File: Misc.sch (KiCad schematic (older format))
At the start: 25 parts, among them U3 PCF8523TK, U4 TLV70218DBV, U5 CDCE913PW, U7 LM75BDP, U8 LM75BDP, X1 32768, X2 20MHz

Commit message: Squiggles! Silk!
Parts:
- renumbered BT1 to BT701, C83 to C701, C84 to C702, C85 to C703, C88 to C704, C86 to C705, C144 to C706, C87 to C707, C123 to C708, C124 to C709, C89 to C710, C142 to C711, C143 to C712, R85 to R701, R88 to R702, R89 to R703, R90 to R704, R91 to R705, U4 to U701, U3 to U702, U7 to U703, U8 to U704, U5 to U705, X2 to X701, X1 to X702

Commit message: Final BOM
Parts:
- added C713, C714: 10p, IPC7351-Nominal:CAPC1005X55, symbol C-0402
- added R706: 1k, IPC7351-Nominal:RESC1005X40, symbol R-0402
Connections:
- net GND: now also C713.2, C714.2
- net at C707.1, U702.3 (VBAT): now also R706.1; no longer BT701.1 (+)
- net at U705.1 (Xin/CLK), X701.1: now also C714.1
- net at U705.14 (Xout), X701.2: now also C713.1
- new net: BT701.1 (+), R706.2
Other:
- moved on the sheet: BT701
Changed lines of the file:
@@
 $EndComp
 $Comp
-L GND #PWR722
+L GND #PWR723
 U 1 1 57983039
 P 6850 1700
-F 0 "#PWR722" H 6850 1700 30  0001 C CNN
+F 0 "#PWR723" H 6850 1700 30  0001 C CNN
 F 1 "GND" H 6850 1630 30  0001 C CNN
 F 2 "" H 6850 1700 60  0000 C CNN
@@
 L BATTERY-SHORT BT701
 U 1 1 579852CE
-P 3800 1800
-F 0 "BT701" H 3940 1821 50  0000 L CNN
-F 1 "3V" H 3940 1730 50  0000 L CNN
-F 2 "manuf:MPD-BU2032SM-HD-G" H 3800 1700 60  0001 C CNN
-F 3 "" H 3800 1700 60  0000 C CNN
-F 4 "DIST DIGIKEY BU2032SM-HD-GCT-ND" H 3800 1800 60  0001 C CNN "BOM"
-	1    3800 1800
+P 3550 1800
+F 0 "BT701" H 3690 1821 50  0000 L CNN
+F 1 "3V" H 3690 1730 50  0000 L CNN
+F 2 "manuf:MPD-BU2032SM-HD-G" H 3550 1700 60  0001 C CNN
+F 3 "" H 3550 1700 60  0000 C CNN
+F 4 "DIST DIGIKEY BU2032SM-HD-GCT-ND" H 3550 1800 60  0001 C CNN "BOM"
+	1    3550 1800
 	1    0    0    -1
 $EndComp
@@
 L GND #PWR708
 U 1 1 5798538F
-P 3800 2000
-F 0 "#PWR708" H 3800 2000 30  0001 C CNN
-F 1 "GND" H 3800 1930 30  0001 C CNN
-F 2 "" H 3800 2000 60  0000 C CNN
-F 3 "" H 3800 2000 60  0000 C CNN
-	1    3800 2000
+P 3550 2000
+F 0 "#PWR708" H 3550 2000 30  0001 C CNN
+F 1 "GND" H 3550 1930 30  0001 C CNN
+F 2 "" H 3550 2000 60  0000 C CNN
+F 3 "" H 3550 2000 60  0000 C CNN
+	1    3550 2000
 	1    0    0    -1
 $EndComp
@@
 CLK_CPU
 $Comp
-L GND #PWR723
+L GND #PWR724
 U 1 1 5798C21D
 P 7900 4100
-F 0 "#PWR723" H 7900 4100 30  0001 C CNN
+F 0 "#PWR724" H 7900 4100 30  0001 C CNN
 F 1 "GND" H 7900 4030 30  0001 C CNN
 F 2 "" H 7900 4100 60  0000 C CNN
@@
 $EndComp
 $Comp
-L GND #PWR724
+L GND #PWR725
 U 1 1 57A157A8
 P 8600 3600
-F 0 "#PWR724" H 8600 3600 30  0001 C CNN
+F 0 "#PWR725" H 8600 3600 30  0001 C CNN
 F 1 "GND" H 8600 3530 30  0001 C CNN
 F 2 "" H 8600 3600 60  0000 C CNN
@@
 $EndComp
 $Comp
-L GND #PWR725
+L GND #PWR726
 U 1 1 57A158A4
 P 8900 3600
-F 0 "#PWR725" H 8900 3600 30  0001 C CNN
+F 0 "#PWR726" H 8900 3600 30  0001 C CNN
 F 1 "GND" H 8900 3530 30  0001 C CNN
 F 2 "" H 8900 3600 60  0000 C CNN
@@
 $EndComp
 $Comp
-L GND #PWR721
+L GND #PWR722
 U 1 1 57A177C2
 P 6350 3250
-F 0 "#PWR721" H 6350 3250 30  0001 C CNN
+F 0 "#PWR722" H 6350 3250 30  0001 C CNN
 F 1 "GND" H 6350 3180 30  0001 C CNN
 F 2 "" H 6350 3250 60  0000 C CNN
@@
 $EndComp
 $Comp
-L GND #PWR719
+L GND #PWR720
 U 1 1 57B04C9B
 P 5800 4200
-F 0 "#PWR719" H 5800 4200 30  0001 C CNN
+F 0 "#PWR720" H 5800 4200 30  0001 C CNN
 F 1 "GND" H 5800 4130 30  0001 C CNN
 F 2 "" H 5800 4200 60  0000 C CNN
@@
 $EndComp
 $Comp
-L GND #PWR720
+L GND #PWR721
 U 1 1 57B04D81
 P 6200 4200
-F 0 "#PWR720" H 6200 4200 30  0001 C CNN
+F 0 "#PWR721" H 6200 4200 30  0001 C CNN
 F 1 "GND" H 6200 4130 30  0001 C CNN
 F 2 "" H 6200 4200 60  0000 C CNN
@@
 L PWR #PWR711
 U 1 1 57B027DE
-P 4600 1650
-F 0 "#PWR711" H 4600 1650 50  0001 C CNN
-F 1 "PWR" H 4600 1650 50  0001 C CNN
-F 2 "" H 4600 1650 60  0000 C CNN
-F 3 "" H 4600 1650 60  0000 C CNN
-	1    4600 1650
+P 4700 1650
+F 0 "#PWR711" H 4700 1650 50  0001 C CNN
+F 1 "PWR" H 4700 1650 50  0001 C CNN
+F 2 "" H 4700 1650 60  0000 C CNN
+F 3 "" H 4700 1650 60  0000 C CNN
+	1    4700 1650
 	-1   0    0    1
 $EndComp
@@
 	4800 1900 4800 2300
 Wire Wire Line
-	3800 1600 5000 1600
-Wire Wire Line
-	3800 1600 3800 1700
-Wire Wire Line
-	3800 2000 3800 1950
+	4150 1600 5000 1600
+Wire Wire Line
+	3550 1600 3550 1700
+Wire Wire Line
+	3550 2000 3550 1950
 Wire Wire Line
 	4300 1700 4300 1600
@@
 	8900 3600 8900 3500
 Wire Wire Line
-	6250 3100 6200 3100
+	6050 3100 6250 3100
 Wire Wire Line
 	6450 3100 6800 3100
@@
 Connection ~ 2200 1500
 Wire Wire Line
-	4600 1650 4600 1600
-Connection ~ 4600 1600
+	4700 1650 4700 1600
+Connection ~ 4700 1600
+$Comp
+L C-0402 C?
+U 1 1 57B0B7B1
+P 5950 2700
+AR Path="/57B0B7B1" Ref="C?"  Part="1"
+AR Path="/5765C2BD/57B0B7B1" Ref="C?"  Part="1"
+AR Path="/57981212/57B0B7B1" Ref="C713"  Part="1"
+F 0 "C713" V 5700 2700 50  0000 C CNN
+F 1 "10p" V 5791 2700 50  0000 C CNN
+F 2 "IPC7351-Nominal:CAPC1005X55" H 5950 2700 50  0001 C CNN
+F 3 "" H 5940 2675 60  0000 C CNN
+F 4 "CAP MLCC 10p C0G [0402]" H 6750 3250 60  0001 C CNN "BOM"
+	1    5950 2700
+	0    1    1    0
+$EndComp
+$Comp
+L C-0402 C?
+U 1 1 57B0B99F
+P 5950 3100
+AR Path="/57B0B99F" Ref="C?"  Part="1"
+AR Path="/5765C2BD/57B0B99F" Ref="C?"  Part="1"
+AR Path="/57981212/57B0B99F" Ref="C714"  Part="1"
+F 0 "C714" V 5700 3100 50  0000 C CNN
+F 1 "10p" V 5791 3100 50  0000 C CNN
+F 2 "IPC7351-Nominal:CAPC1005X55" H 5950 3100 50  0001 C CNN
+F 3 "" H 5940 3075 60  0000 C CNN
+F 4 "CAP MLCC 10p C0G [0402]" H 6750 3650 60  0001 C CNN "BOM"
+	1    5950 3100
+	0    1    1    0
+$EndComp
+Connection ~ 6200 3100
+Wire Wire Line
+	6050 2700 6550 2700
+Wire Wire Line
+	6550 2700 6550 3100
+Connection ~ 6550 3100
+Wire Wire Line
+	5850 2700 5750 2700
+Wire Wire Line
+	5750 2700 5750 3100
+Wire Wire Line
+	5750 3100 5850 3100
+$Comp
+L GND #PWR719
+U 1 1 57B0BDB7
+P 5650 2900
+F 0 "#PWR719" H 5650 2900 30  0001 C CNN
+F 1 "GND" H 5650 2830 30  0001 C CNN
+F 2 "" H 5650 2900 60  0000 C CNN
+F 3 "" H 5650 2900 60  0000 C CNN
+	1    5650 2900
+	0    1    1    0
+$EndComp
+Wire Wire Line
+	5650 2900 5750 2900
+Connection ~ 5750 2900
+$Comp
+L R-0402 R706
+U 1 1 57B0F234
+P 4050 1600
+F 0 "R706" V 4158 1600 50  0000 C CNN
+F 1 "1k" V 4249 1600 50  0000 C CNN
+F 2 "IPC7351-Nominal:RESC1005X40" H 4050 1600 50  0001 C CNN
+F 3 "" H 4050 1650 60  0000 C CNN
+F 4 "RES SMD 1k 1% [0402]" H 4800 2150 60  0001 C CNN "BOM"
+	1    4050 1600
+	0    1    1    0
+$EndComp
+Wire Wire Line
+	3950 1600 3550 1600
 $EndSCHEMATC

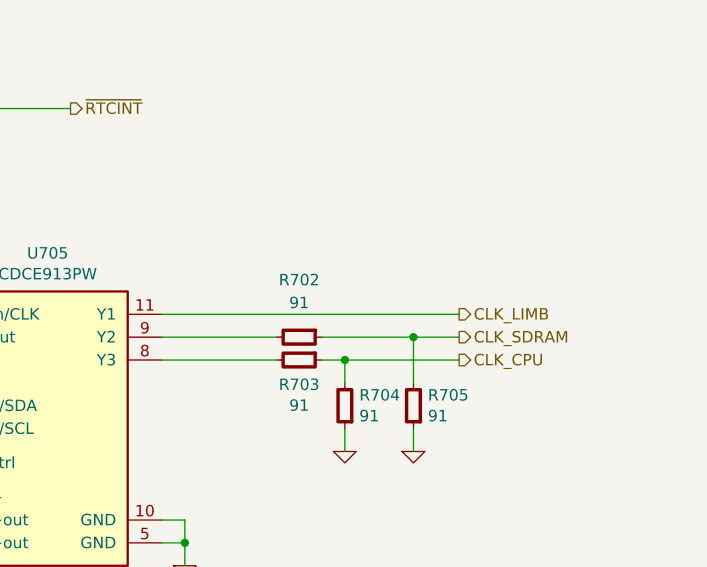
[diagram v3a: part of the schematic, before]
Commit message: Add some test points
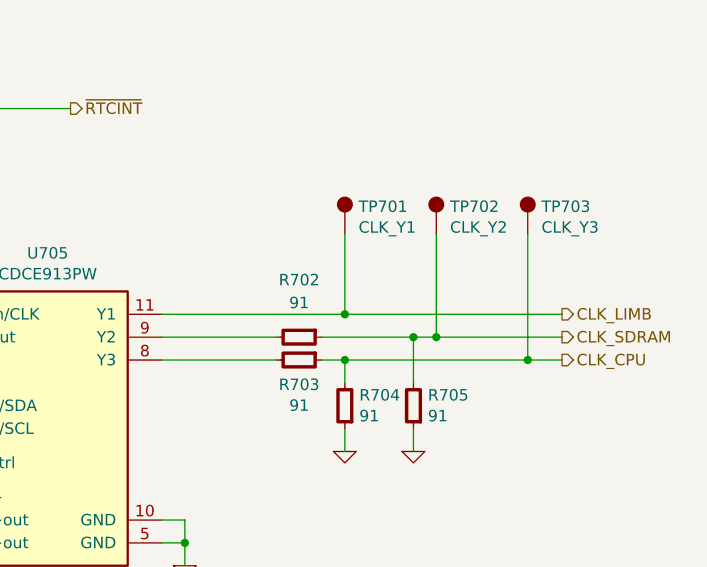
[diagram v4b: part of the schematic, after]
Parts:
- added TP701: CLK_Y1, conn-test:TEST-SMD-SMALL, symbol TESTPOINT
- added TP702: CLK_Y2, conn-test:TEST-SMD-SMALL, symbol TESTPOINT
- added TP703: CLK_Y3, conn-test:TEST-SMD-SMALL, symbol TESTPOINT
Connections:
- net CLK_CPU: now also TP703.1
- net CLK_LIMB: now also TP701.1
- net CLK_SDRAM: now also TP702.1
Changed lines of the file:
@@
 	1    0    0    -1
 $EndComp
-Text HLabel 9100 3000 2    50   Output ~ 0
+Text HLabel 9550 3000 2    50   Output ~ 0
 CLK_LIMB
-Text HLabel 9100 3100 2    50   Output ~ 0
+Text HLabel 9550 3100 2    50   Output ~ 0
 CLK_SDRAM
-Text HLabel 9100 3200 2    50   Output ~ 0
+Text HLabel 9550 3200 2    50   Output ~ 0
 CLK_CPU
 $Comp
@@
 	4800 6700 4800 6600
 Wire Wire Line
-	7800 3000 9100 3000
+	7800 3000 9550 3000
 Wire Wire Line
 	8300 3100 7800 3100
 Wire Wire Line
-	8500 3100 9100 3100
-Wire Wire Line
-	8500 3200 9100 3200
+	8500 3100 9550 3100
+Wire Wire Line
+	8500 3200 9550 3200
 Wire Wire Line
 	8300 3200 7800 3200
@@
 Wire Wire Line
 	3950 1600 3550 1600
+$Comp
+L TESTPOINT TP701
+U 1 1 57C83404
+P 8600 2650
+F 0 "TP701" H 8660 2771 50  0000 L CNN
+F 1 "CLK_Y1" H 8660 2680 50  0000 L CNN
+F 2 "conn-test:TEST-SMD-SMALL" H 8600 2650 50  0001 C CNN
+F 3 "" H 8600 2650 50  0000 C CNN
+	1    8600 2650
+	1    0    0    -1
+$EndComp
+Wire Wire Line
+	8600 2650 8600 3000
+Connection ~ 8600 3000
+$Comp
+L TESTPOINT TP702
+U 1 1 57C83706
+P 9000 2650
+F 0 "TP702" H 9060 2771 50  0000 L CNN
+F 1 "CLK_Y2" H 9060 2680 50  0000 L CNN
+F 2 "conn-test:TEST-SMD-SMALL" H 9000 2650 50  0001 C CNN
+F 3 "" H 9000 2650 50  0000 C CNN
+	1    9000 2650
+	1    0    0    -1
+$EndComp
+$Comp
+L TESTPOINT TP703
+U 1 1 57C8377C
+P 9400 2650
+F 0 "TP703" H 9460 2771 50  0000 L CNN
+F 1 "CLK_Y3" H 9460 2680 50  0000 L CNN
+F 2 "conn-test:TEST-SMD-SMALL" H 9400 2650 50  0001 C CNN
+F 3 "" H 9400 2650 50  0000 C CNN
+	1    9400 2650
+	1    0    0    -1
+$EndComp
+Wire Wire Line
+	9000 2650 9000 3100
+Connection ~ 9000 3100
+Wire Wire Line
+	9400 2650 9400 3200
+Connection ~ 9400 3200
 $EndSCHEMATC

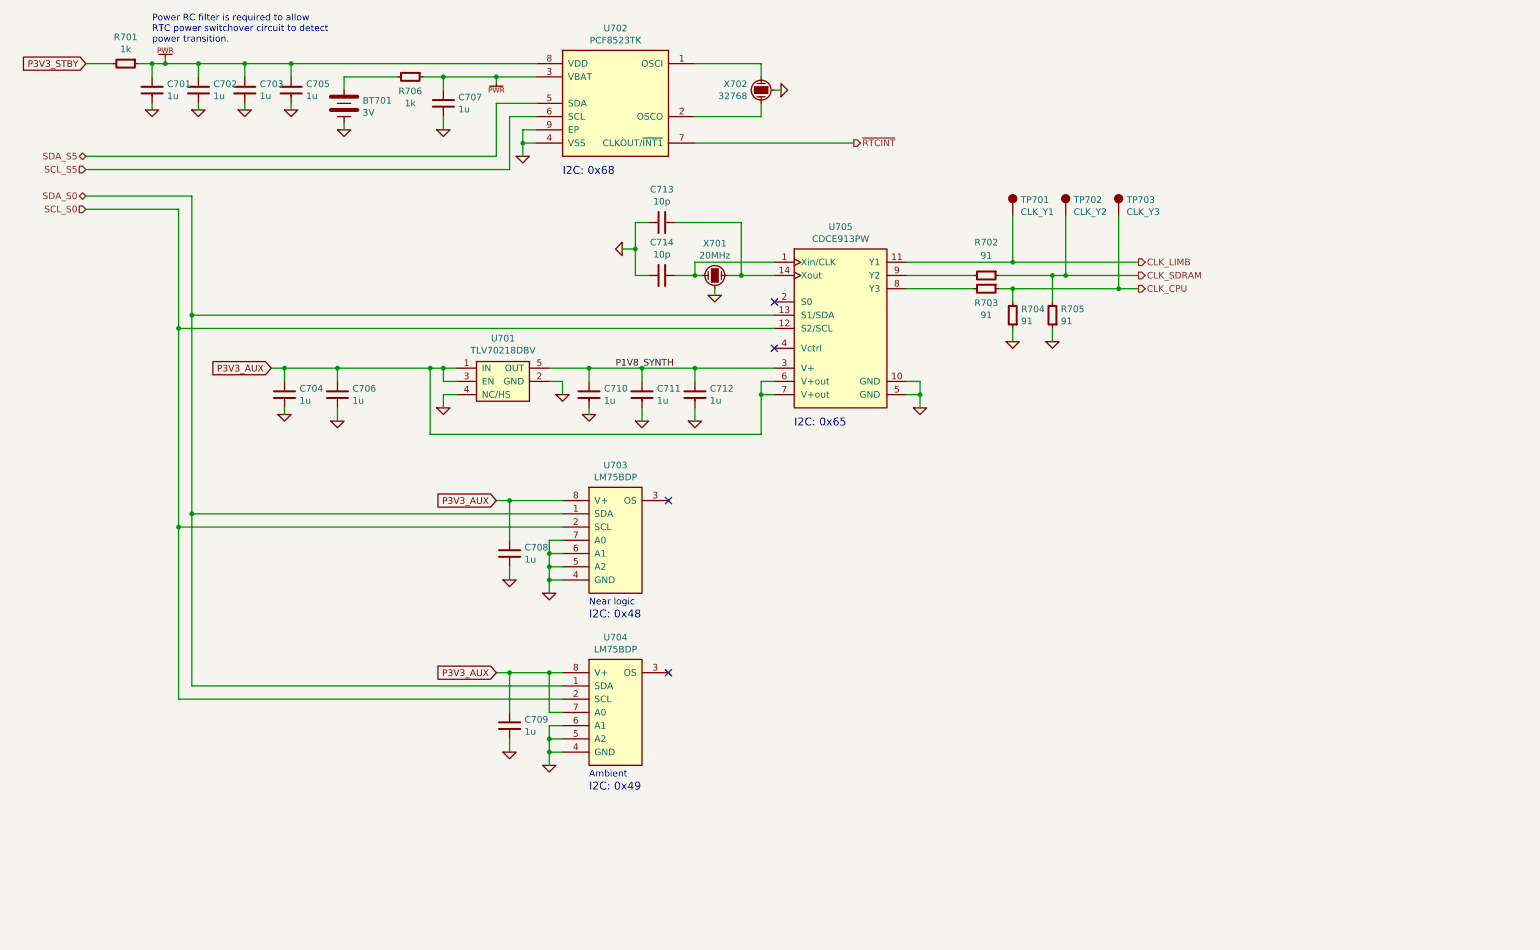
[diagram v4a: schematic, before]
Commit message: Tidy schematics and produce PDF
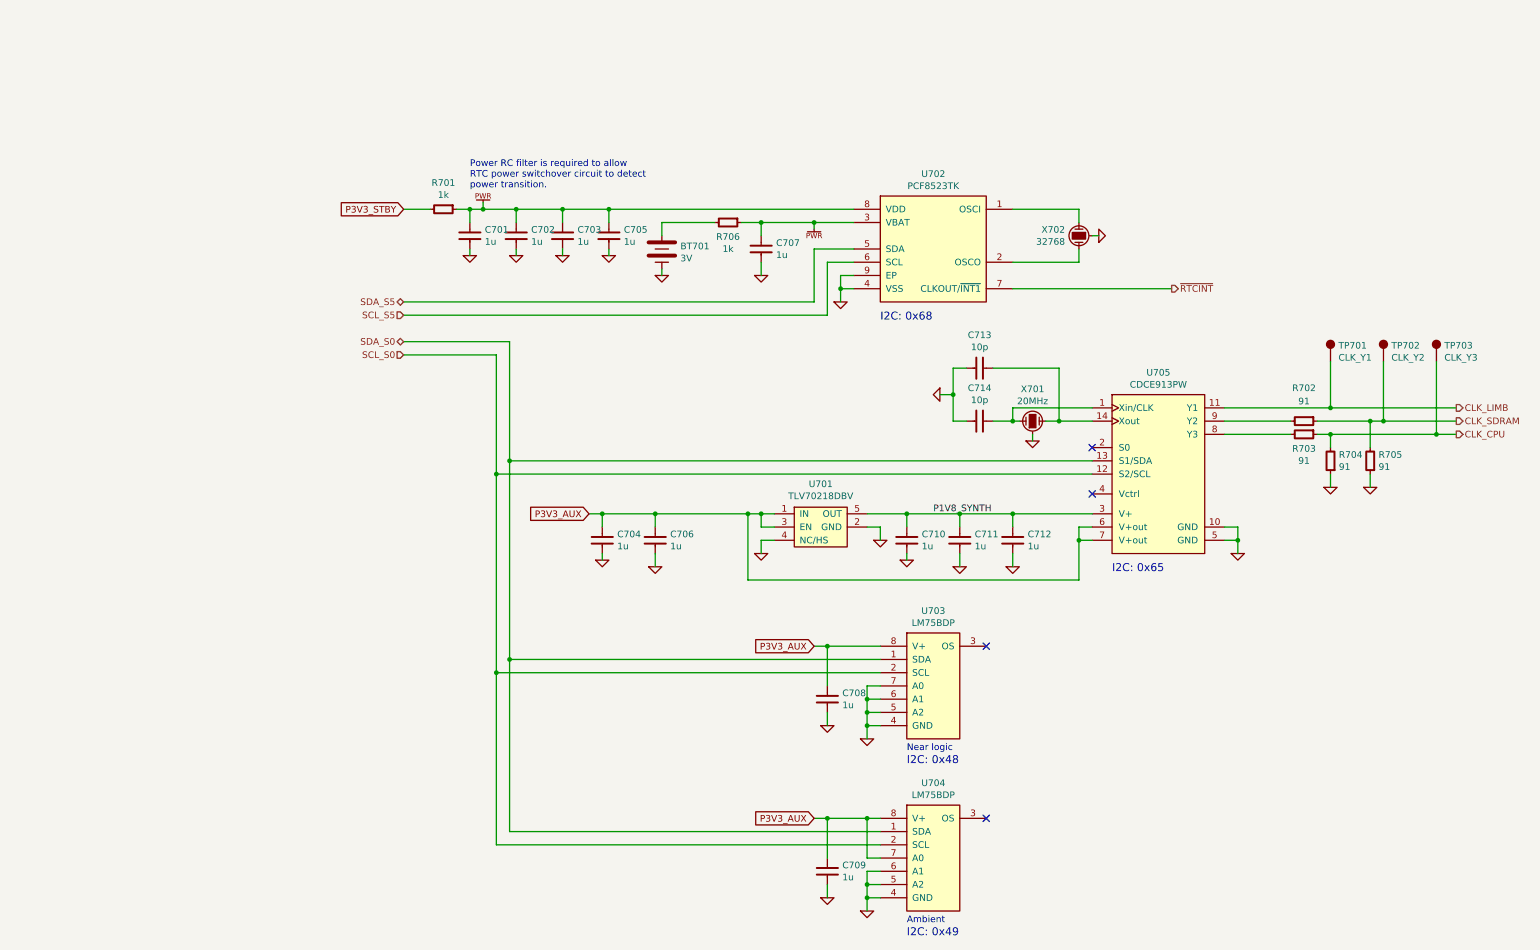
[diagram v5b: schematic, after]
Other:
- moved on the sheet: BT701, C701, C702, C703, C704, C705, C706, C707, C708, C709, C710, C711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

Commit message: Update for KiCad 5
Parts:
- BT701: symbol BATTERY-SHORT -> _passive:BATTERY-SHORT
- C701, C702, C703, C704, C705, C706, C707, C708, C709, C710, C711, C712, C713, C714: symbol C-0402 -> pasv-cap:C-0402
- R701, R702, R703, R704, R705, R706: symbol R-0402 -> pasv-res:R-0402
- TP701, TP702, TP703: symbol TESTPOINT -> pcb:TESTPOINT
- U701: symbol TLV702vvDBV -> TexasInstruments:TLV702vvDBV
- U702: symbol PCF8523TK -> NXP:PCF8523TK
- U703, U704: symbol LM75BDP -> NXP:LM75BDP
- U705: symbol CDCE913PW -> TexasInstruments:CDCE913PW
- X701: symbol XTAL-ABRACON-ABM8G -> pasv-xtal:XTAL-ABRACON-ABM8G
- X702: symbol XTAL-CITIZEN-CM130 -> pasv-xtal:XTAL-CITIZEN-CM130

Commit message: Fix IO expanders (symbol changed in library)
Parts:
- U703, U704: symbol NXP:LM75BDP -> motherboard-rescue:LM75BDP-RESCUE-motherboard
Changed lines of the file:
@@
 $EndComp
 $Comp
-L NXP:LM75BDP U703
+L motherboard-rescue:LM75BDP-RESCUE-motherboard U703
 U 1 1 579F4ACE
 P 8000 5900
@@
 NoConn ~ 8400 5900
 $Comp
-L NXP:LM75BDP U704
+L motherboard-rescue:LM75BDP-RESCUE-motherboard U704
 U 1 1 579F50E6
 P 8000 7200
